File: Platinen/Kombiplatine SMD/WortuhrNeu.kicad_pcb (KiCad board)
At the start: 2 copper layers, 339 x 40.5 mm, 100 parts, among them J1 Conn_01x01_Pin, J2 PROG MODE, J3 UART FLOATING, J4 UART, J5 Eingangsbuchse, SW1 PTS645Vx83-2LFS, SW2 PTS645Vx83-2LFS, U2 MCP1826-ADJE/ET, U3 Bluepill, U4 DS18B20, U6 Arduino_Nano_Every, U7 ESP-07, U8 Generic DCDC, U9 TP582, X1 Conn_01x03_Pin, X10 Conn_01x03_Pin, X11 Conn_01x03_Pin, X12 Conn_01x03_Pin, X13 Conn_01x03_Pin, X14 Conn_01x03_Pin, X15 Conn_01x03_Pin, X16 Conn_01x03_Pin, X17 Conn_01x03_Pin, X18 Conn_01x03_Pin, X19 Conn_01x03_Pin, X2 Conn_01x03_Pin, X20 Conn_01x03_Pin, X21 Conn_01x03_Pin, X22 Conn_01x03_Pin, X23 Conn_01x03_Pin, X24 Conn_01x03_Pin, X25 Conn_01x03_Pin, X26 Conn_01x03_Pin, X27 Conn_01x03_Pin, X28 Conn_01x03_Pin, X29 Conn_01x03_Pin, X3 Conn_01x03_Pin, X30 Conn_01x03_Pin, X31 Conn_01x03_Pin, X32 Conn_01x03_Pin, X33 Conn_01x03_Pin, X34 Conn_01x03_Pin, X35 Conn_01x03_Pin, X36 Conn_01x03_Pin, X37 Conn_01x03_Pin, X38 Conn_01x03_Pin, X4 Conn_01x03_Pin, X5 Conn_01x03_Pin, X6 Conn_01x03_Pin, X7 Conn_01x03_Pin, X8 Conn_01x03_Pin, X9 Conn_01x03_Pin

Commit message: Implement some of the changes requested in issue 1
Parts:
- removed H7, H8, H9: MountingHole, MountingHole:MountingHole_3.2mm_M3_DIN965
- added H5: MountingHole, MountingHole:MountingHole_3.2mm_M3_DIN965, F.Cu at (46.1, 176.7)
- moved H6 328.4 mm to (374.5, 176.1)
- moved H4 289.9 mm to (376.2, 144.8)
- moved H3 203.9 mm to (352.3, 152.0)
- moved H2 141.4 mm to (235.1, 157.5)
- moved U5 2.30 mm to (236.6, 157.0)
- moved U6 0.75 mm to (214.2, 149.3)
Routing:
- net SDA: track 27.3 -> 29.6 mm
- net SCL: track 28.0 -> 30.3 mm
- net GND: track 83.0 -> 81.0 mm, vias 66 -> 64
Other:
- board text added: "USB"

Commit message: Changes to Kombiplatine THT
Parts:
- J1: footprint TestPoint:TestPoint_Pad_1.0x1.0mm -> Connector_PinHeader_1.00mm:PinHeader_1x01_P1.00mm_Vertical
- moved C14 1.75 mm to (252.9, 159.5)
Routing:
- net +5V: track 639.3 -> 645.1 mm, vias 6 -> 7
- net GND: track 81.0 -> 86.5 mm, vias 64 -> 66
- net +3V3: track 295.7 -> 296.6 mm

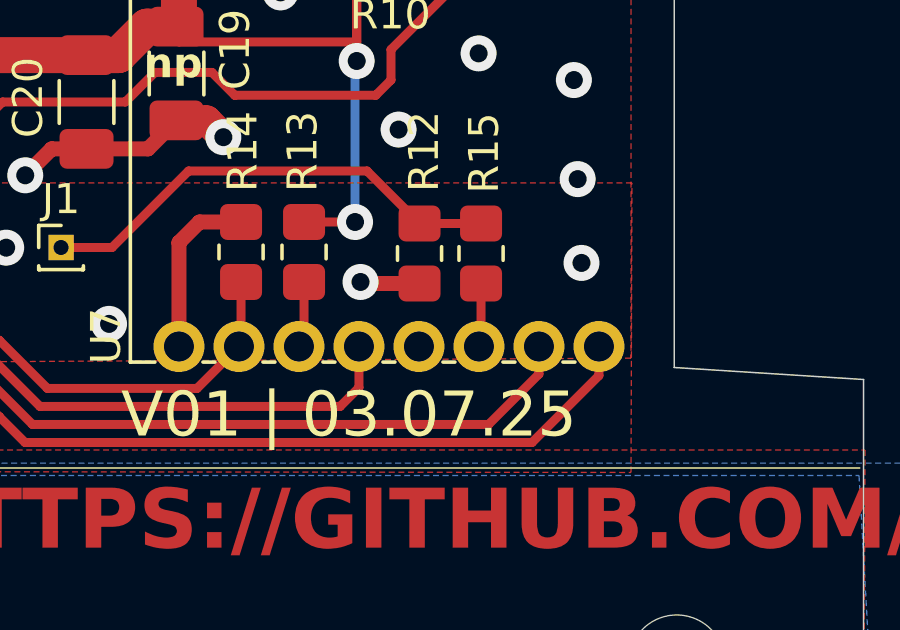
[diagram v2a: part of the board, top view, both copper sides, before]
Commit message: Switched gpio4&5 on the esp for both boards
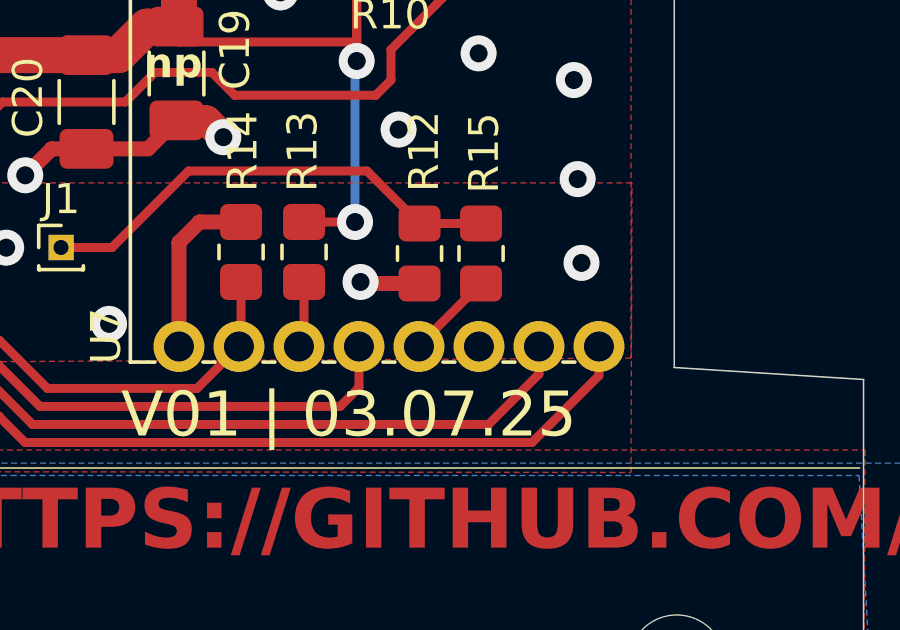
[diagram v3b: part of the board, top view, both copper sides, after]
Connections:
- R15 pad 2: Net-(U7-GPIO5) -> Net-(U7-GPIO4)
- U7 pad 13: unconnected-(U7-GPIO4-Pad13) -> Net-(U7-GPIO4)
- U7 pad 14: Net-(U7-GPIO5) -> unconnected-(U7-GPIO5-Pad14)
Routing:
- net Net-(U7-GPIO4): track 0.00 -> 2.96 mm
- net Net-(U7-GPIO5): track 2.13 -> 0.00 mm

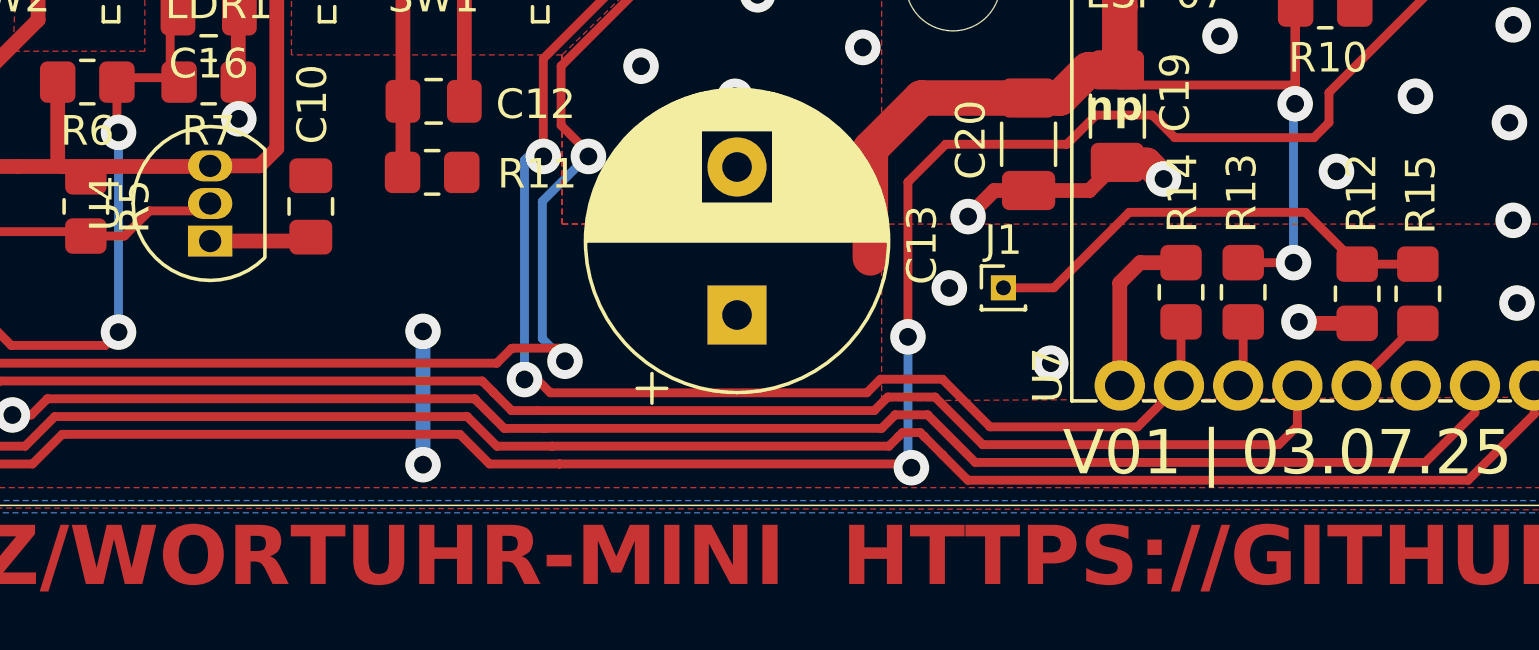
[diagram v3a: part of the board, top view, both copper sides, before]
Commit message: Moved J1 closer to STM32 for OTA cable(SMD)
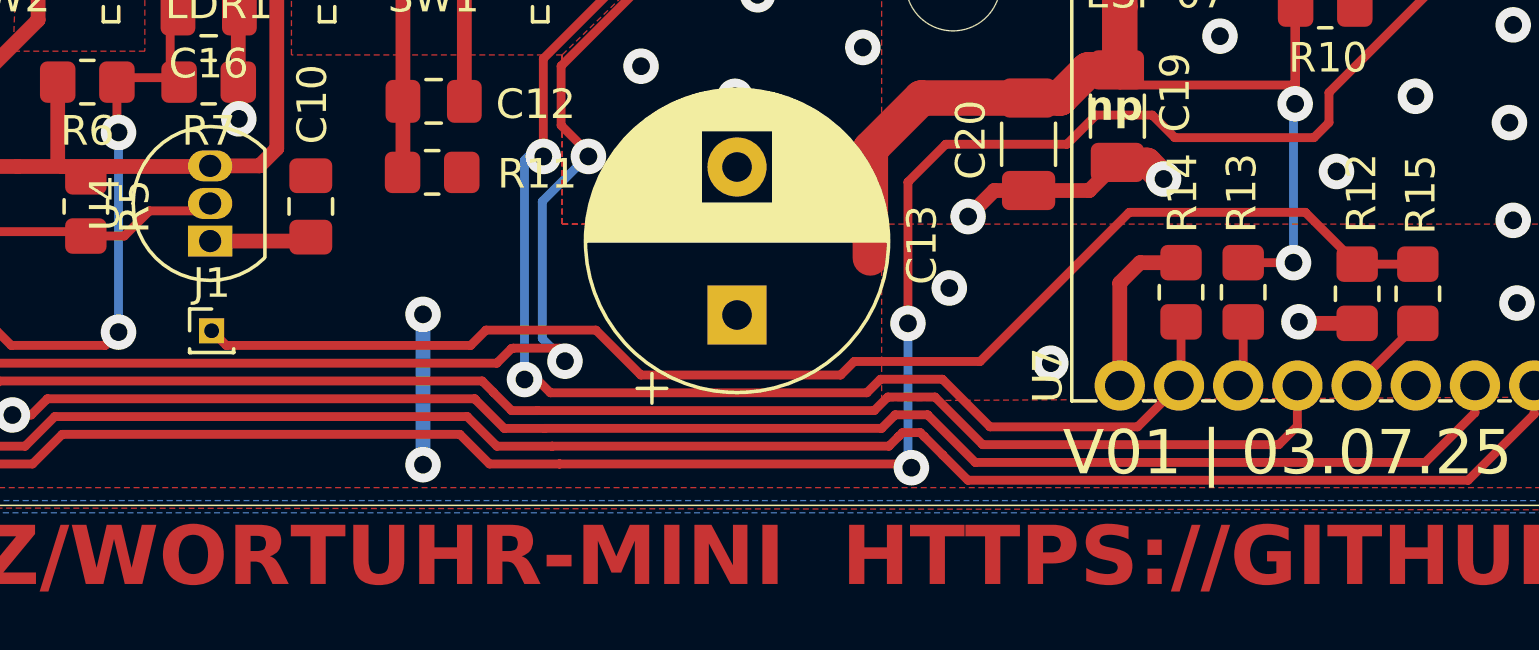
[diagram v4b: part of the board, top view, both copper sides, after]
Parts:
- moved J1 26.8 mm to (327.2, 163.8)
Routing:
- net Net-(J1-Pin_1): track 15.8 -> 44.8 mm
- net +3V3: track 296.6 -> 297.2 mm
